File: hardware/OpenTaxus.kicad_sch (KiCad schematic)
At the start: 56 parts, among them J1 OLED, J2 qwiic, J3 SWD, J4 USB_C_Receptacle_USB2.0, J5 connector, Q2 BC847BS, Q3 PT12-21B/TR8, SW1 dpad, SW2 USB_BOOT, SW3 RESET, SW4 SW_SPDT, SW5 USB_BOOT, U1 HE6206-33NR, U2 W25Q128JVS, U3 RP2040, U4 XT1861B332MR-G, Y1 YSX321SL

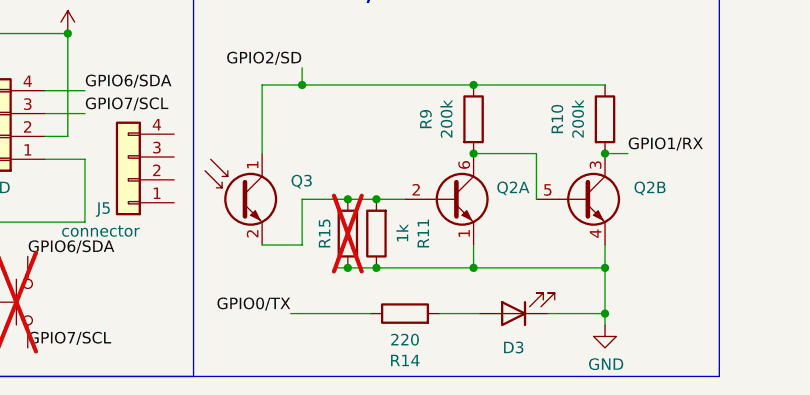
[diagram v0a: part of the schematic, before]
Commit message: Fine tuning R11 and R14 so badges can communicate up to 1 inch apart.
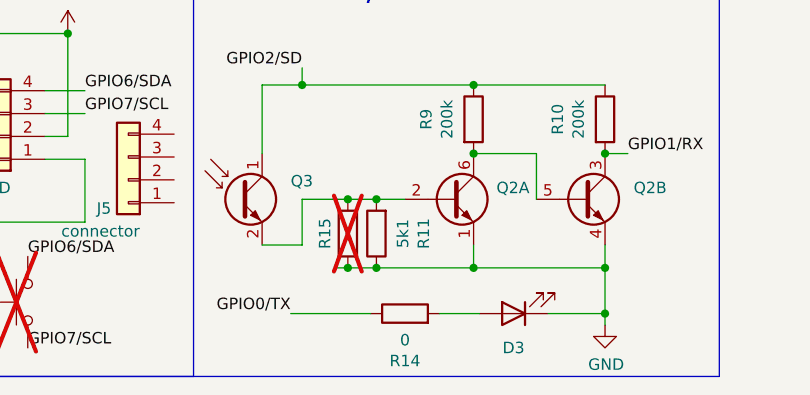
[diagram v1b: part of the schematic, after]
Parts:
- R11: value 1k -> 5k1; LCSC C11702 -> C25941; P/N 0402WGF1001TCE -> 0402WGJ0512TCE
- R14: value 220 -> 0; LCSC C25091 -> C17168; P/N 0402WGF2200TCE -> 0402WGF0000TCE
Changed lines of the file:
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@@
 			)
 		)
-		(property "Value" "1k"
+		(property "Value" "5k1"
 			(at 142.0114 182.245 90)
 			(effects
@@
 			)
 		)
-		(property "LCSC" "C11702"
+		(property "LCSC" "C25941"
 			(at 139.065 182.245 0)
 			(effects
@@
 			)
 		)
-		(property "P/N" "0402WGF1001TCE"
+		(property "P/N" "0402WGJ0512TCE"
 			(at 139.065 182.245 0)
 			(effects
@@
 			)
 		)
-		(property "Value" "220"
+		(property "Value" "0"
 			(at 142.24 194.0814 90)
 			(effects
@@
 			)
 		)
-		(property "LCSC" "C25091"
+		(property "LCSC" "C17168"
 			(at 142.24 191.135 0)
 			(effects
@@
 			)
 		)
-		(property "P/N" "0402WGF2200TCE"
+		(property "P/N" "0402WGF0000TCE"
 			(at 142.24 191.135 0)
 			(effects
